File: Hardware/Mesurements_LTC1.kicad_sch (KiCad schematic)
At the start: 12 parts, among them Q1 NPN, U1 BQ79614PAPRQ1

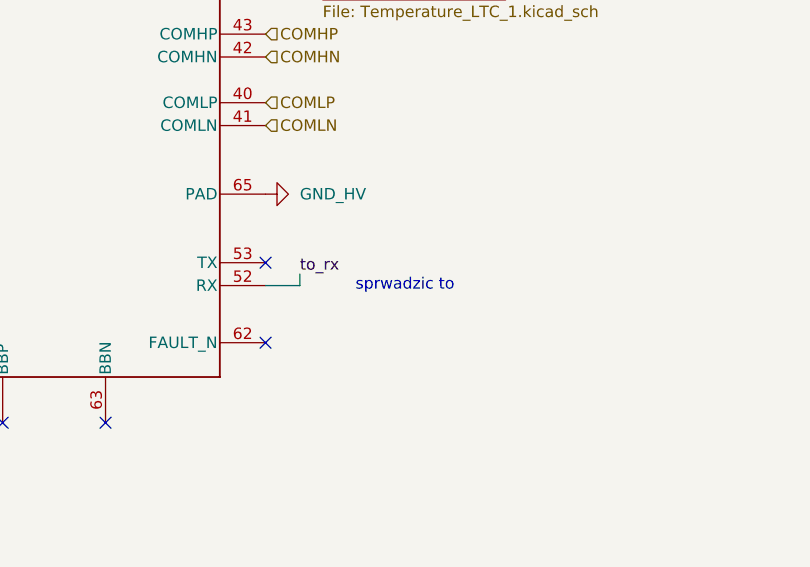
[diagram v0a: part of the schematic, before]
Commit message: Dodano diody TVS na każdej części zasilania, zmieniono bezpieczniki, podzielono bezpieczniki na bezpieczniki do prądów wewnętrznych oraz zewnętrznych,poprawiono małe błedy
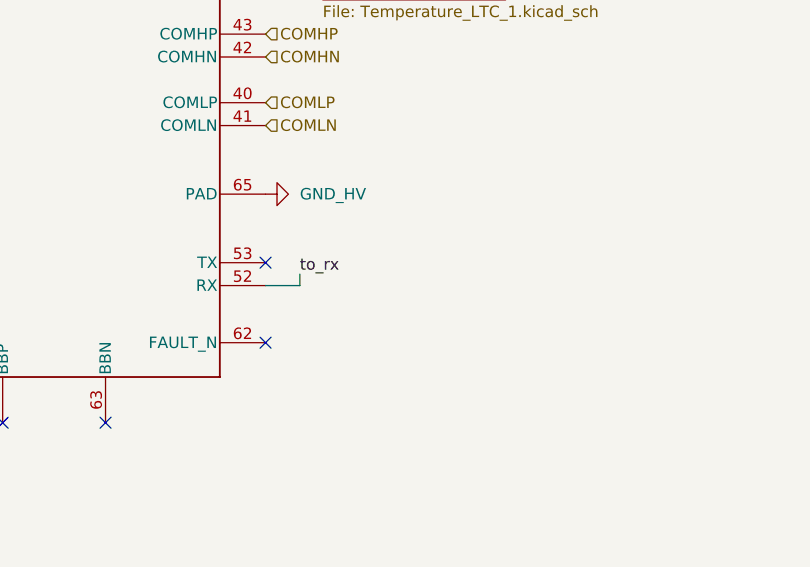
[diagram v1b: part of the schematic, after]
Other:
- note removed: "sprwadzic to"
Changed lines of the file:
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@@
-		)
-	)
-	(text "sprwadzic to\n"
-		(exclude_from_sim no)
-		(at 137.414 134.62 0)
-		(effects
-			(font
-				(size 1.27 1.27)
-			)
 		)
 	)

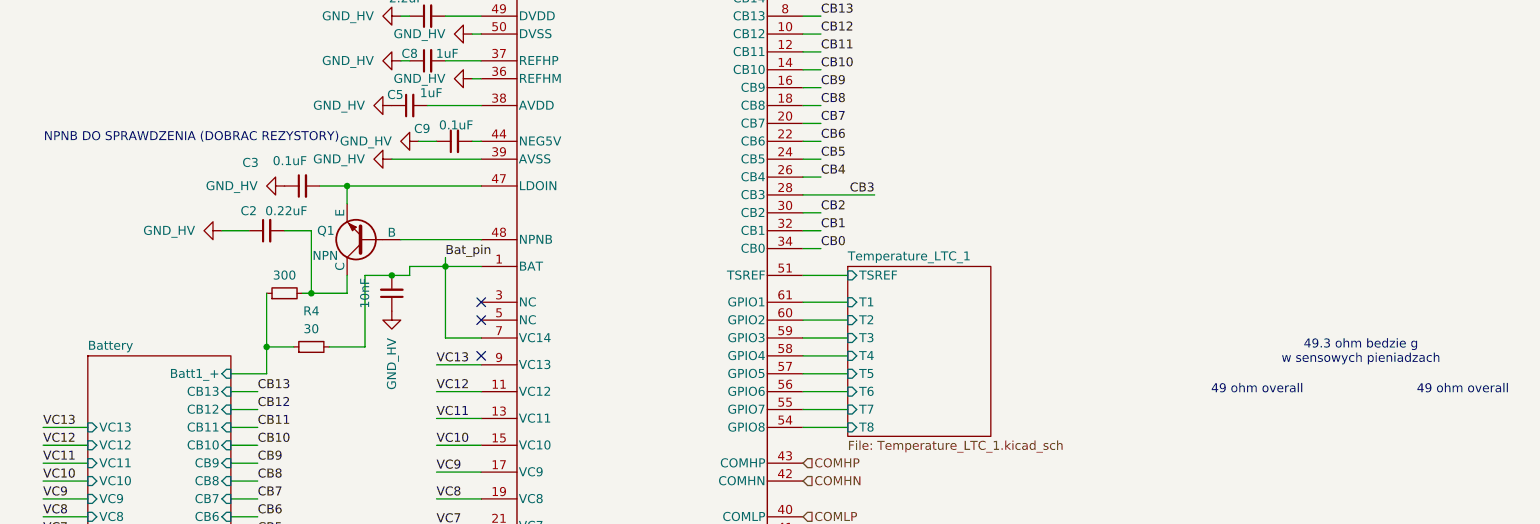
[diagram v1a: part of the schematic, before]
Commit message: dodano pozostale datasheety, zmieniono blad w usb
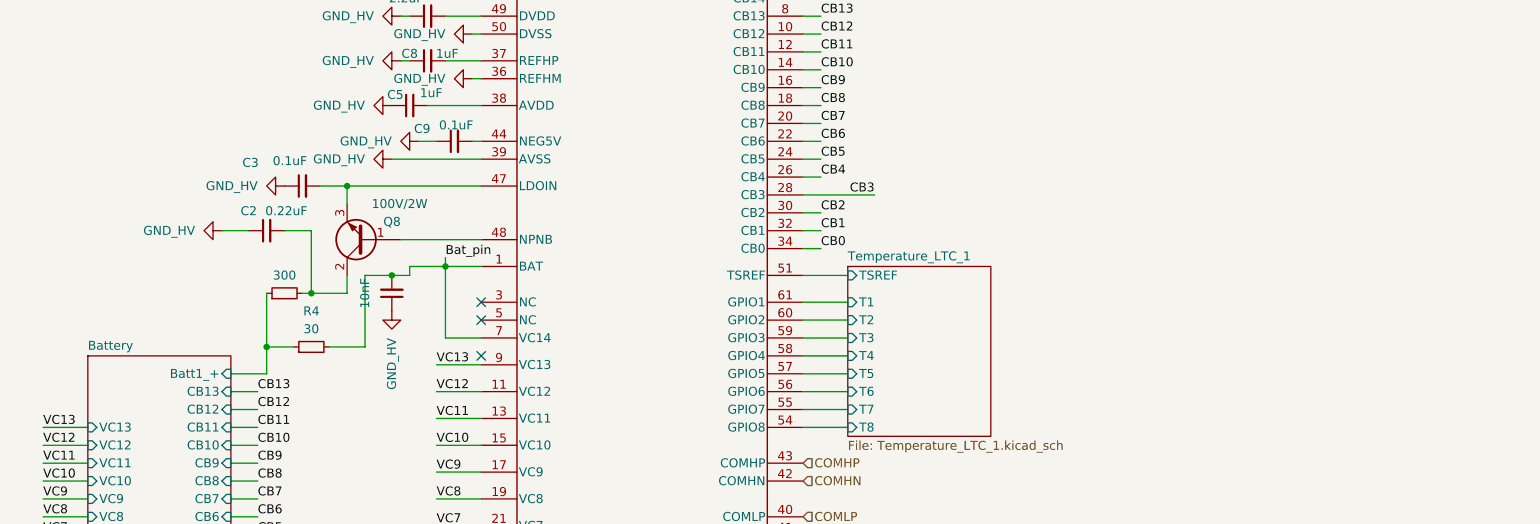
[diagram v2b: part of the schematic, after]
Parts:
- removed Q1: NPN, Package_TO_SOT_SMD:SOT-223-3_TabPin2, symbol Simulation_SPICE:NPN
- added Q8: 100V/2W, Package_TO_SOT_SMD:SOT-223-3_TabPin2, symbol Device:Q_NPN_BCE
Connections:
- net at C2.2, R2.2: now also Q8.2 (C)
- net at C3.2, U1.47 (LDOIN): now also Q8.3 (E)
- net at U1.48 (NPNB): now also Q8.1 (B)
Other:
- note removed: "49 ohm overall"
- note removed: "49.3 ohm bedzie g w sensowych pieniadzach"
- note removed: "NPNB DO SPRAWDZENIA (DOBRAC REZYSTORY)"
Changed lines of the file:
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@@
 	(generator_version "9.0")
 	(paper "A4")
-	(text "49.3 ohm bedzie g\nw sensowych pieniadzach"
-		(exclude_from_sim no)
-		(at 201.168 90.932 0)
-		(effects
-			(font
-				(size 1.27 1.27)
-			)
-		)
-	)
-	(text "49 ohm overall\n"
-		(exclude_from_sim no)
-		(at 215.646 96.266 0)
-		(effects
-			(font
-				(size 1.27 1.27)
-			)
-		)
-	)
-	(text "49 ohm overall\n"
-		(exclude_from_sim no)
-		(at 186.436 96.266 0)
-		(effects
-			(font
-				(size 1.27 1.27)
-			)
-		)
-	)
-	(text "NPNB DO SPRAWDZENIA (DOBRAC REZYSTORY)\n"
-		(exclude_from_sim no)
-		(at 35.052 60.452 0)
-		(effects
-			(font
-				(size 1.27 1.27)
-			)
-		)
-	)
 	(junction
 		(at 57.15 67.31)
@@
 				(path "/26289bb6-56bc-4ca1-b1a2-18d58d1afdf5/329d2a9a-b359-4d8c-80ce-edb0b764c6b7"
 					(reference "#PWR020")
+					(unit 1)
+				)
+			)
+		)
+	)
+	(symbol
+		(lib_id "Device:Q_NPN_BCE")
+		(at 59.69 74.93 180)
+		(unit 1)
+		(exclude_from_sim no)
+		(in_bom yes)
+		(on_board yes)
+		(dnp no)
+		(property "Reference" "Q8"
+			(at 64.77 72.39 0)
+			(effects
+				(font
+					(size 1.27 1.27)
+				)
+				(justify left)
+			)
+		)
+		(property "Value" "100V/2W"
+			(at 68.58 69.85 0)
+			(effects
+				(font
+					(size 1.27 1.27)
+				)
+				(justify left)
+			)
+		)
+		(property "Footprint" "Package_TO_SOT_SMD:SOT-223-3_TabPin2"
+			(at 54.61 77.47 0)
+			(effects
+				(font
+					(size 1.27 1.27)
+				)
+				(hide yes)
+			)
+		)
+		(property "Datasheet" "https://eu.mouser.com/ProductDetail/Diodes-Incorporated/FZT653TA?qs=rI7uf1IzohQqmHMCtqURKQ%3D%3D"
+			(at 59.69 74.93 0)
+			(effects
+				(font
+					(size 1.27 1.27)
+				)
+				(hide yes)
+			)
+		)
+		(property "Description" "NPN transistor, base/collector/emitter"
+			(at 59.69 74.93 0)
+			(effects
+				(font
+					(size 1.27 1.27)
+				)
+				(hide yes)
+			)
+		)
+		(property "TME Electronic Components Part Number" ""
+			(at 59.69 74.93 0)
+			(effects
+				(font
+					(size 1.27 1.27)
+				)
+				(hide yes)
+			)
+		)
+		(property "TME Electronic Components Price/Stock" ""
+			(at 59.69 74.93 0)
+			(effects
+				(font
+					(size 1.27 1.27)
+				)
+				(hide yes)
+			)
+		)
+		(property "Arrow Part Number" ""
+			(at 59.69 74.93 0)
+			(effects
+				(font
+					(size 1.27 1.27)
+				)
+				(hide yes)
+			)
+		)
+		(property "Arrow Price/Stock" ""
+			(at 59.69 74.93 0)
+			(effects
+				(font
+					(size 1.27 1.27)
+				)
+				(hide yes)
+			)
+		)
+		(property "Mouser Part Number" "522-FZT653TA"
+			(at 59.69 74.93 0)
+			(effects
+				(font
+					(size 1.27 1.27)
+				)
+				(hide yes)
+			)
+		)
+		(pin "1"
+		)
+		(pin "3"
+		)
+		(pin "2"
+		)
+		(instances
+			(project "BMS"
+				(path "/26289bb6-56bc-4ca1-b1a2-18d58d1afdf5/329d2a9a-b359-4d8c-80ce-edb0b764c6b7"
+					(reference "Q8")
 					(unit 1)
 				)
@@
 	)
 	(symbol
-		(lib_id "Simulation_SPICE:NPN")
-		(at 59.69 74.93 180)
-		(unit 1)
-		(exclude_from_sim no)
-		(in_bom yes)
-		(on_board yes)
-		(dnp no)
-		(property "Reference" "Q1"
-			(at 55.372 73.66 0)
-			(effects
-				(font
-					(size 1.27 1.27)
-				)
-				(justify left)
-			)
-		)
-		(property "Value" "NPN"
-			(at 55.88 77.216 0)
-			(effects
-				(font
-					(size 1.27 1.27)
-				)
-				(justify left)
-			)
-		)
-		(property "Footprint" "Package_TO_SOT_SMD:SOT-223-3_TabPin2"
-			(at -3.81 74.93 0)
-			(effects
-				(font
-					(size 1.27 1.27)
-				)
-				(hide yes)
-			)
-		)
-		(property "Datasheet" "https://eu.mouser.com/c/semiconductors/discrete-semiconductors/transistors/?collector-%20base%20voltage%20vcbo=100%20V&collector-%20emitter%20voltage%20vceo%20max=80%20V&mounting%20style=SMD%2FSMT&transistor%20polarity=NPN"
-			(at -3.81 74.93 0)
-			(effects
-				(font
-					(size 1.27 1.27)
-				)
-				(hide yes)
-			)
-		)
-		(property "Description" "NPN"
-			(at 59.69 74.93 0)
-			(effects
-				(font
-					(size 1.27 1.27)
-				)
-				(hide yes)
-			)
-		)
-		(property "opis" "NPN"
-			(at 59.69 74.93 0)
-			(effects
-				(font
-					(size 1.27 1.27)
-				)
-				(hide yes)
-			)
-		)
-		(property "Sim.Type" "GUMMELPOON"
-			(at 59.69 74.93 0)
-			(effects
-				(font
-					(size 1.27 1.27)
-				)
-				(hide yes)
-			)
-		)
-		(property "Sim.Pins" "1=C 2=B 3=E"
-			(at 59.69 74.93 0)
-			(effects
-				(font
-					(size 1.27 1.27)
-				)
-				(hide yes)
-			)
-		)
-		(pin "1"
-		)
-		(pin "2"
-		)
-		(pin "3"
-		)
-		(instances
-			(project "BMS"
-				(path "/26289bb6-56bc-4ca1-b1a2-18d58d1afdf5/329d2a9a-b359-4d8c-80ce-edb0b764c6b7"
-					(reference "Q1")
-					(unit 1)
-				)
-			)
-		)
-	)
-	(symbol
 		(lib_id "Device:C_Small")
 		(at 68.58 49.53 90)
@@
 			)
 		)
-		(property "Datasheet" "BQ79616PAPRQ1"
+		(property "Datasheet" "https://www.ti.com/product/BQ79614-Q1/part-details/BQ79614PAPRQ1"
 			(at 99.06 87.63 0)
 			(effects

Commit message: Wersja V1.0 gotowa, wysłana do produckji
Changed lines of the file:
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@@
 	(wire
 		(pts
-			(xy 121.92 134.62) (xy 125.73 134.62)
+			(xy 121.92 134.62) (xy 124.46 134.62)
 		)
 		(stroke
@@
 		(pts
 			(xy 121.92 71.12) (xy 124.46 71.12)
-		)
-		(stroke
-			(width 0)
-			(type default)
-		)
-	)
-	(wire
-		(pts
-			(xy 125.73 133.35) (xy 125.73 134.62)
 		)
 		(stroke
@@
 	)
 	(label "to_rx"
-		(at 125.73 133.35 0)
-		(effects
-			(font
+		(at 124.46 134.62 0)
+		(effects
+			(font

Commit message: Male zmiany
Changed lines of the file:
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@@
 	(wire
 		(pts
-			(xy 121.92 68.58) (xy 132.08 68.58)
+			(xy 121.92 68.58) (xy 128.27 68.58)
 		)
 		(stroke
@@
 	)
 	(label "CB3"
-		(at 132.08 68.58 180)
-		(effects
-			(font
+		(at 128.27 68.58 180)
+		(effects
+			(font

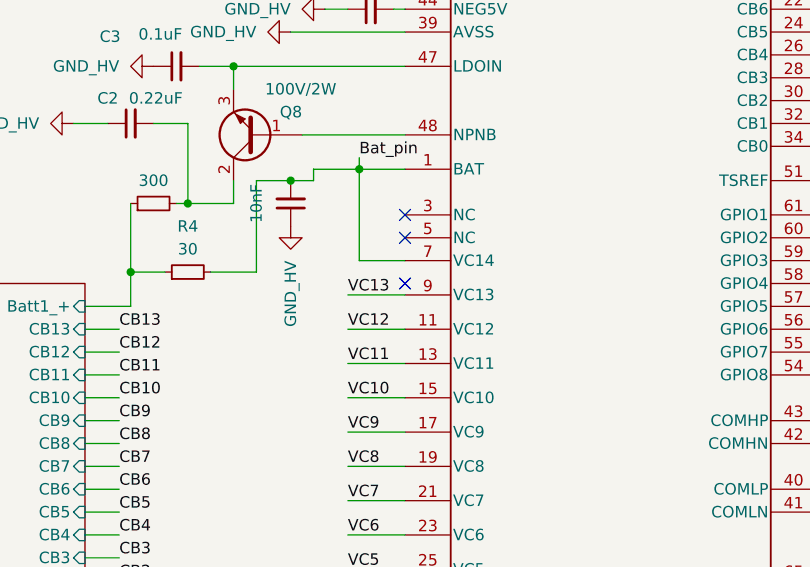
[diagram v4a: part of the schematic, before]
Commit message: Dodano podstawy komunikacji CAN , nie przeprowadzono jescze weryfikacji działania kodu
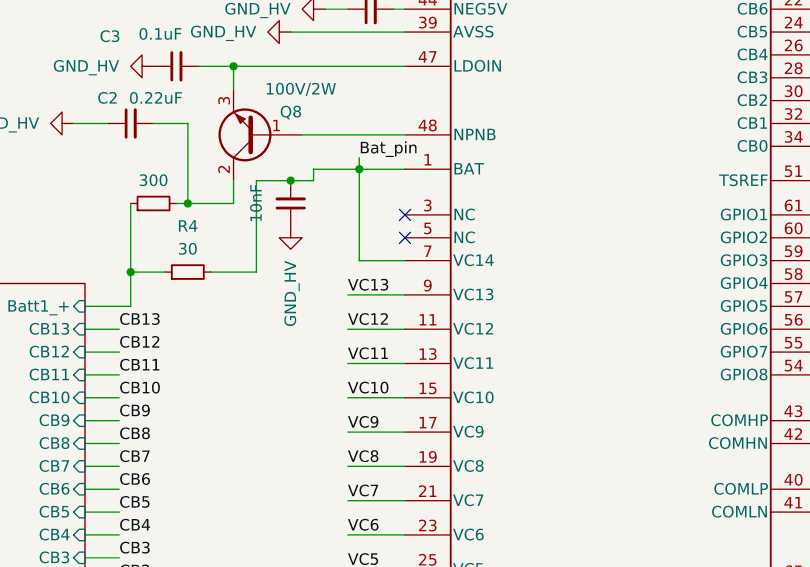
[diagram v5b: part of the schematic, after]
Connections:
- no-connect marks 9 -> 8
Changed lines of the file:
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@@
-	)
-	(no_connect
-		(at 76.2 91.44)
 	)
 	(no_connect

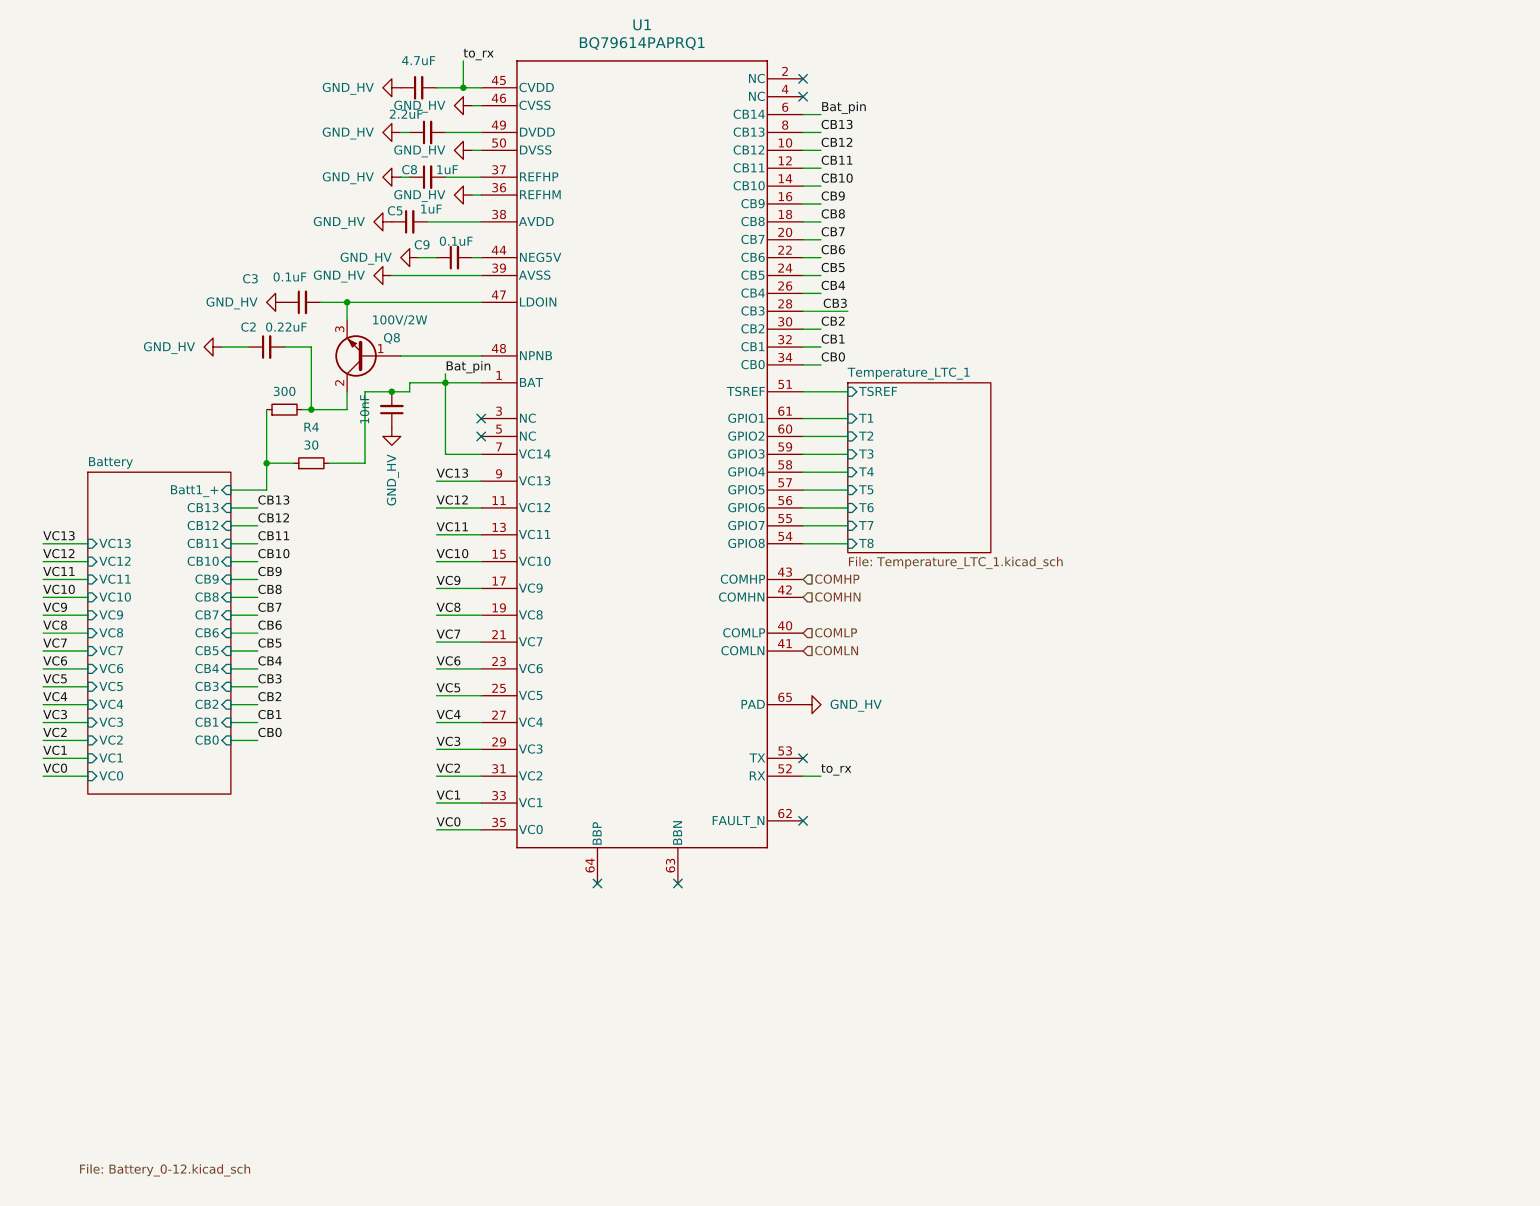
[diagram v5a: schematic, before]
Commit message: Zmiany wizualne w schemacie
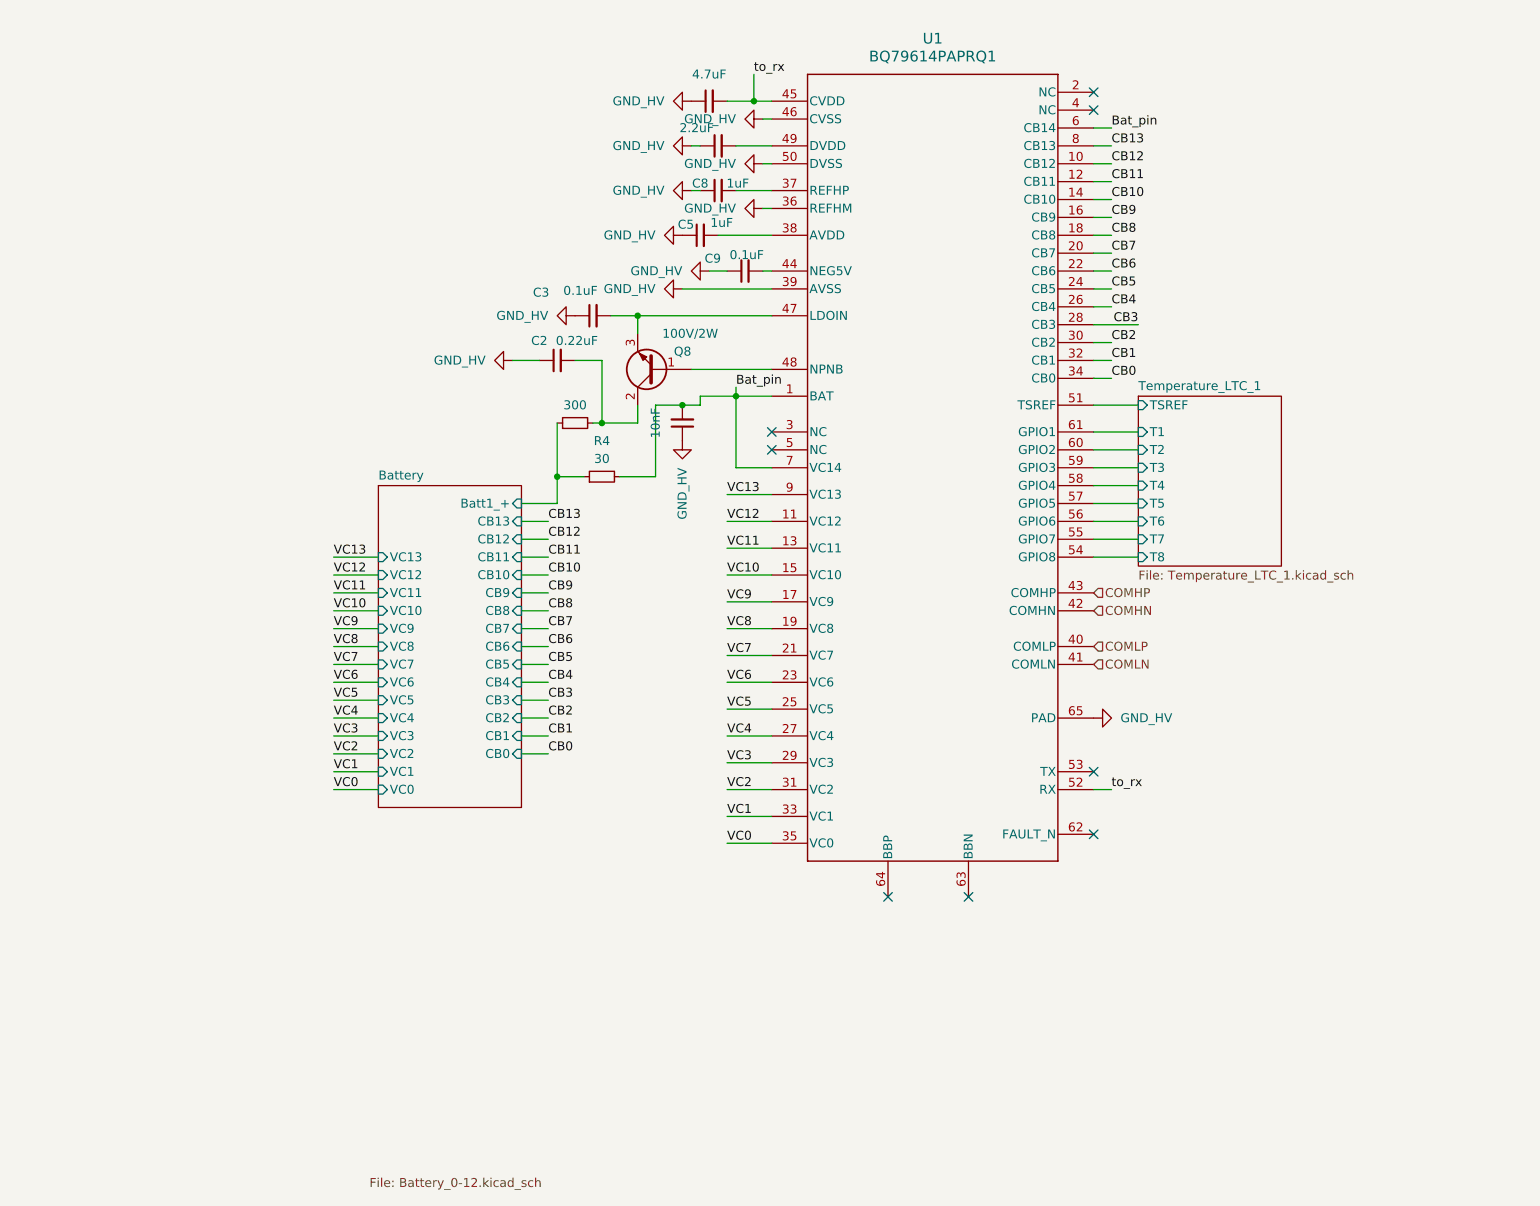
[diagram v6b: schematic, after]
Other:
- moved on the sheet: C2, C3, C5, C8, C9, Q8, R4, U1
